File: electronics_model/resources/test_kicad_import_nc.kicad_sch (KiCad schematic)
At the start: 3 parts

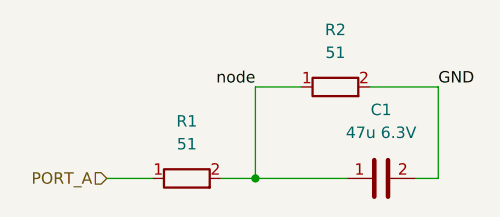
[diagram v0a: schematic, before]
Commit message: Schematic import improvements (#238)
- More checks to the import flow:
- Detect disconnected labels and error on those (since the import flow
can't detect connections mid-wire)
- Not-connected checks if there's no pins connected or >1 pins connected
(NC must be connected to exactly one pin)
- Note, not-connected is not required (should this change in the
future?)
- Refactor the import flow:
- Power pins are treated as pseudolabels, since they don't show up on
component symbols list
- Shared connected-components algorithm that takes a list of list of
connected components and merges all the sublists that overlap in terms
of components
- Two stage import flow: first stage to connect wire points, then second
stage connects tunnels
  - After the first stage, we can check for disconnected labels
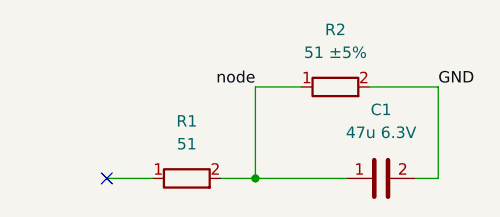
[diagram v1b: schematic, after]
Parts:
- R2: value 51 -> 51 ±5%
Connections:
- net PORT_A: no longer names the net of R1.1
- no-connect marks 0 -> 1
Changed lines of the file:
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@@
   (junction (at 91.44 96.52) (diameter 0) (color 0 0 0 0)
   )
+  (no_connect (at 74.93 96.52))
   (wire (pts (xy 91.44 86.36) (xy 91.44 96.52))
     (stroke (width 0) (type default) (color 0 0 0 0))
@@
     (effects (font (size 1.27 1.27)) (justify left bottom))
   )
-  (hierarchical_label "PORT_A" (shape input) (at 74.93 96.52 180)
-    (effects (font (size 1.27 1.27)) (justify right))
-  )
   (symbol (lib_id "Device:R") (at 83.82 96.52 90) (unit 1)
     (in_bom yes) (on_board yes) (fields_autoplaced)
@@
     (in_bom yes) (on_board yes) (fields_autoplaced)
     (property "Reference" "R2" (id 0) (at 100.33 80.01 90))
-    (property "Value" "51" (id 1) (at 100.33 82.55 90))
+    (property "Value" "51 ±5%" (id 1) (at 100.33 82.55 90))
     (property "Footprint" "" (id 2) (at 100.33 88.138 90)
       (effects (font (size 1.27 1.27)) hide)
@@
     )
     (path "/a8f9f58a-4aa6-48fb-915f-461e000613f8"
-      (reference "R2") (unit 1) (value "51") (footprint "")
+      (reference "R2") (unit 1) (value "51 ±5%") (footprint "")
     )
   )
